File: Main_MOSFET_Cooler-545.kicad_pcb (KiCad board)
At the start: 2 copper layers, 100 x 100 mm, 20 parts, among them J1 Gate, J2 MOS-, J3 MOS+, J4 Thermister, P1 Eoshi-chan_Silk, P2 Serial_QR, Q1 TK100E06N1, Q2 TK100E06N1

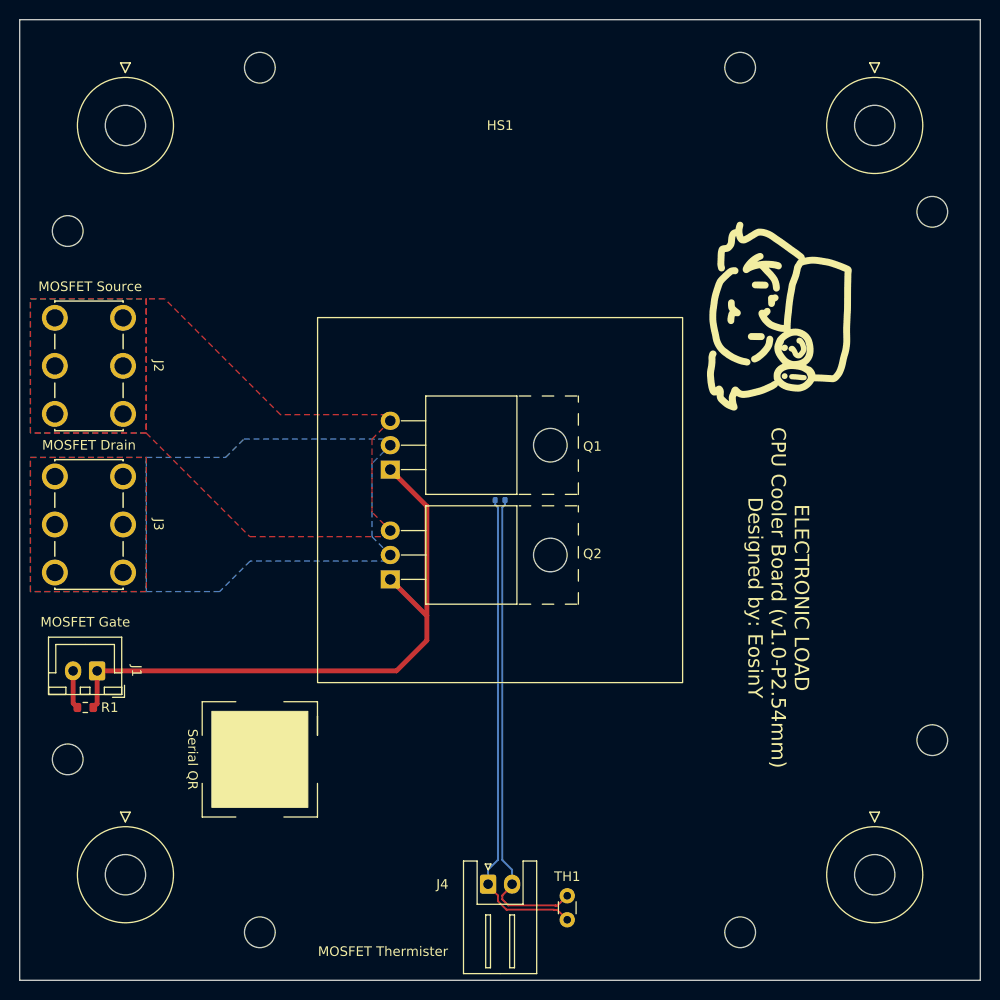
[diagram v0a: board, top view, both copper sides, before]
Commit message: added 5.45mm pitch version
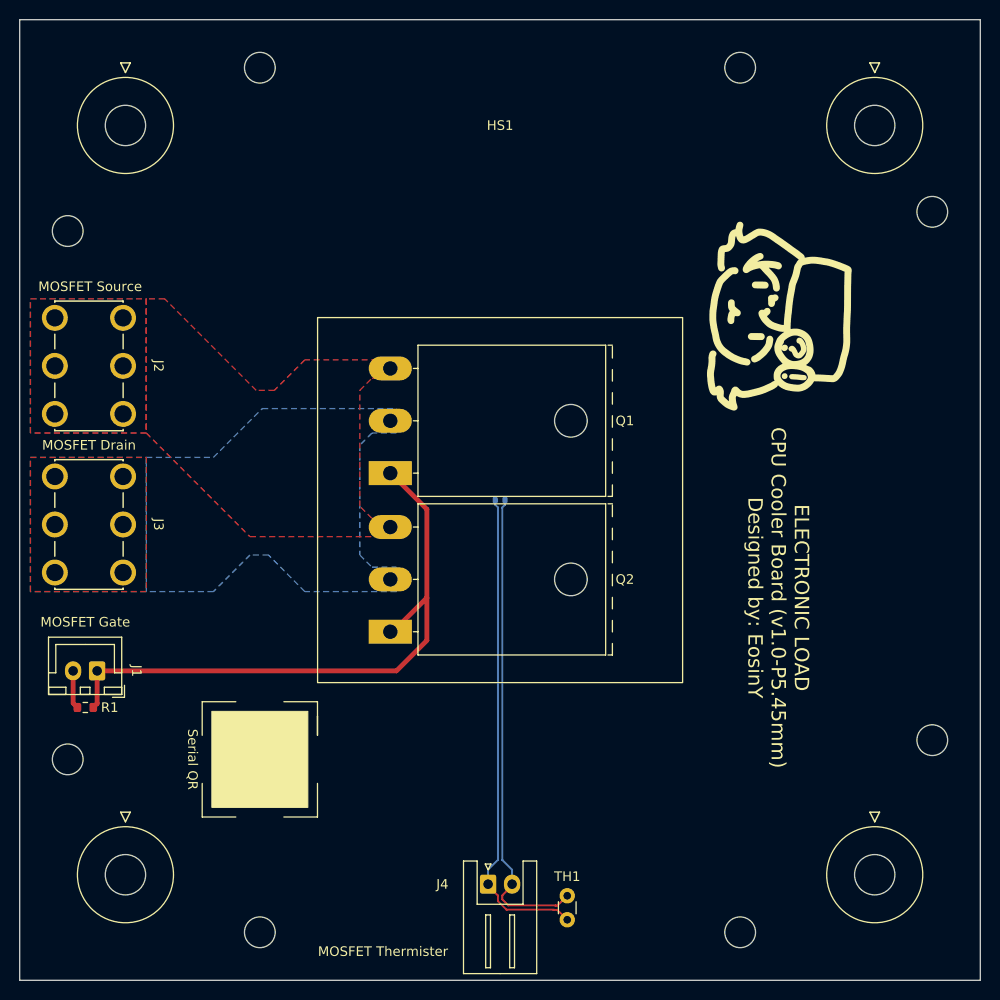
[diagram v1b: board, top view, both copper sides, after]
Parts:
- Q1, Q2: footprint Package_TO_SOT_THT:TO-220-3_Horizontal_TabUp -> Package_TO_SOT_THT:TO-3P-3_Horizontal_TabUp
- moved Q2 5.45 mm to (68.6, 93.7)
- moved Q1 0.37 mm to (68.6, 77.2)
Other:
- board text added: "ELECTRONIC LOAD CPU Cooler Board (v1.0-P5.45mm) Designed by: EosinY"
- board text removed: "ELECTRONIC LOAD CPU Cooler Board (v1.0-P2.54mm) Designed by: EosinY"
